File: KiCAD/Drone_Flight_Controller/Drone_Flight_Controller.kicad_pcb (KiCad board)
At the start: 2 copper layers, 85 x 45 mm, 104 parts, among them J201 Conn_01x04, J205 XT60, J207 Conn_01x05, P601 USB_C_Plug_USB2.0, Q201 BC846C, Q202 BC856C, Q203 BC846C, Q204 BC856C, Q205 BC846C, Q206 BC856C, Q207 BC846C, Q208 BC856C, Q401 2N2222A, Q601 BC846C, Q602 BC846C, Q603 BC846C, Q604 BC846C, Q605 BC846C, Q606 BC846C, Q607 BC846C, SW301 SW_Push, U201 AS358, U202 AS358, U205 AS358, U301 DPS368, U302 BNO055, U303 ESP32-WROOM-32, U601 MCP2200-I-SO, U701 LM2576-3.3WT, Y601 CSTNE12M0GH5L000R0

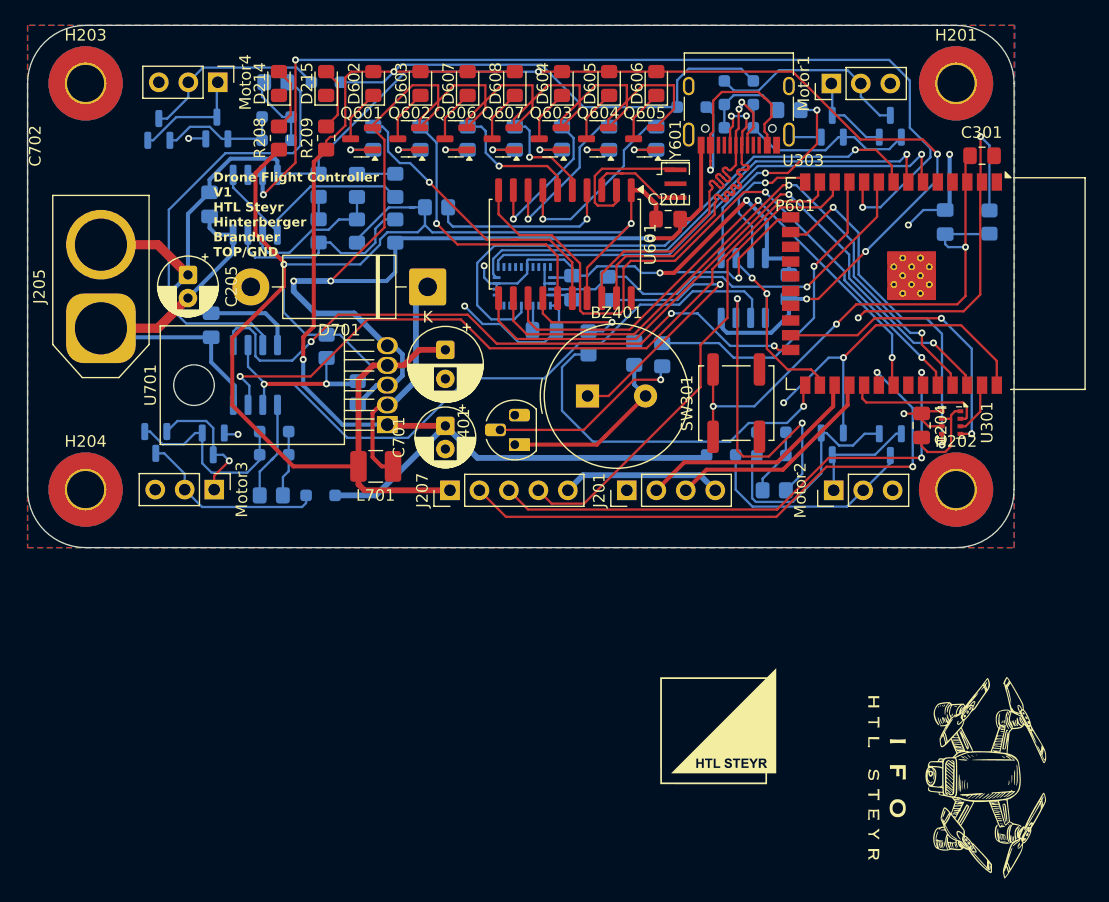
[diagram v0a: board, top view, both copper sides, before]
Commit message: bottom GND and USB C port
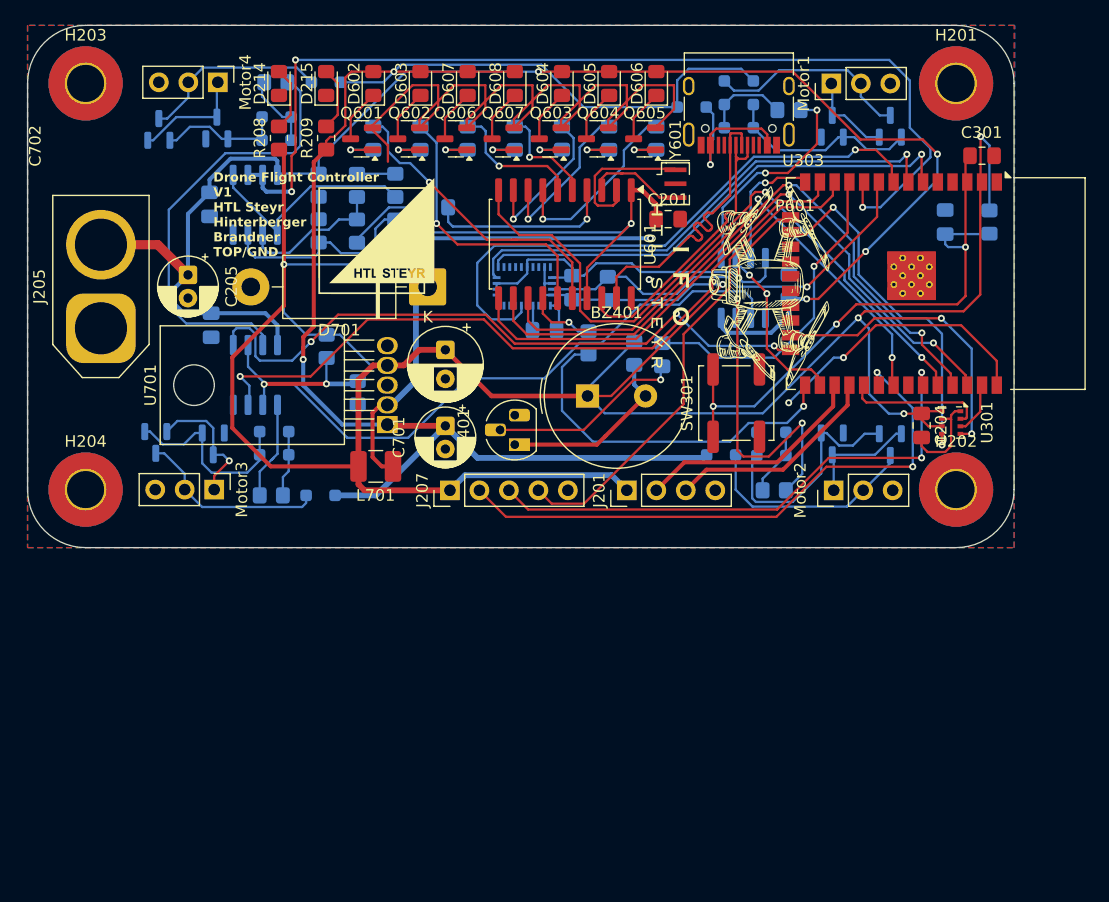
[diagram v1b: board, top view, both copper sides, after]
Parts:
- moved G*** 51.5 mm to (98.0, 93.2)
- moved G*** 46.3 mm to (129.3, 97.3)
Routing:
- net GND: track 325.2 -> 176.3 mm, vias 14 -> 5
- net +3V3: track 204.5 -> 282.0 mm
- net Net-(U601-D-): track 33.2 -> 25.4 mm, vias 2 -> 0
- net Net-(D601-A): track 21.5 -> 14.1 mm
- net Net-(U601-D+): track 31.5 -> 25.9 mm, vias 2 -> 0
- net ~{Programming}: track 9.96 -> 5.89 mm
- net Programming TX: track 60.4 -> 59.2 mm
- net Motor1: track 12.3 -> 11.2 mm
- net BATT Monitor: track 86.5 -> 87.3 mm
- added copper zone on B.Cu, net GND
- removed copper zone on B.Cu, net +3V3

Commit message: add IFO picture and HTL Logo
add IFO picture and HTL Logo
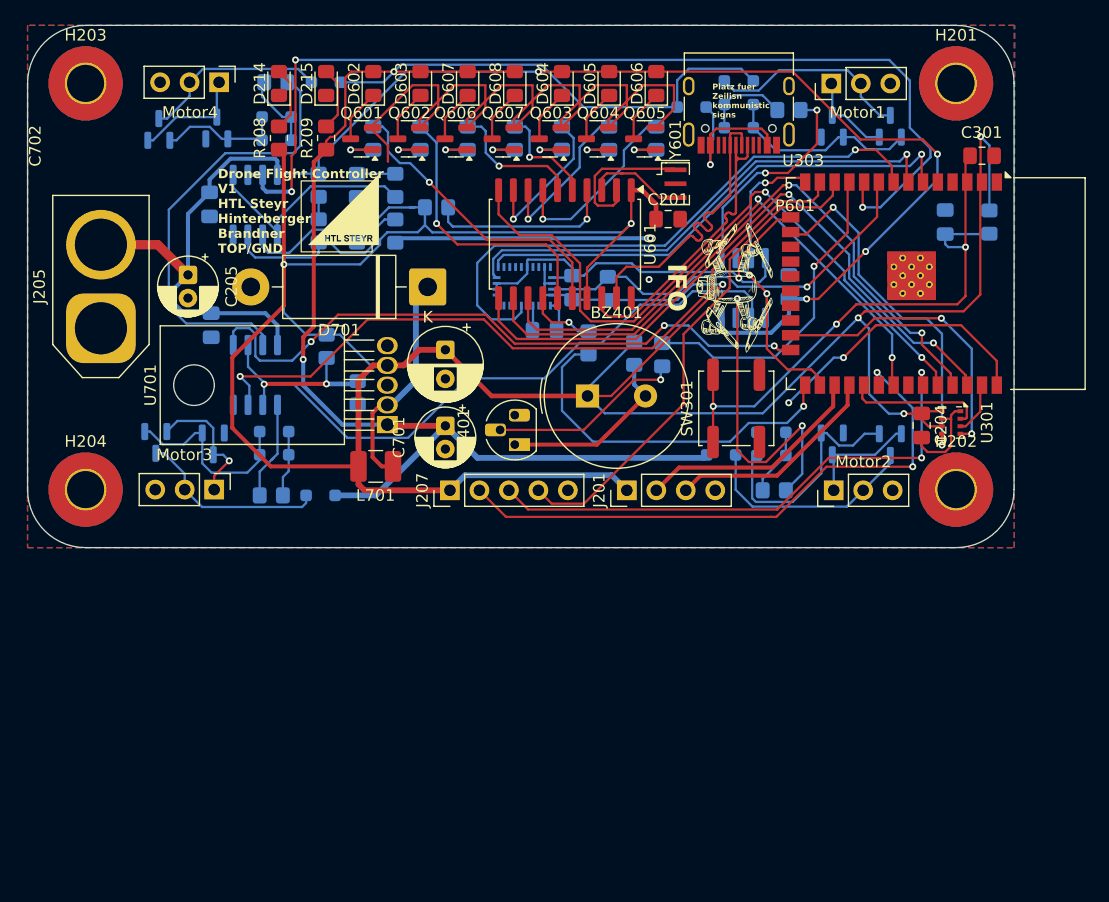
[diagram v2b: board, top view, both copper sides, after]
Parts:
- removed G*** (x2): LOGO, LOGO
- moved SW301 0.45 mm to (129.1, 108.0)
- moved Motor4 0.11 mm to (84.5, 79.9)
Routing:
- net Motor4: track 56.6 -> 55.8 mm
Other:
- board text added: "IFO"
- board text added: "Platz fuer Zeilisn kommunistic signs"

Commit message: Connector and ESP placement
Connector and ESP placement
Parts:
- moved Motor3 0.58 mm to (83.5, 115.0)
- moved U303 0.25 mm to (143.2, 97.5)
- moved Motor1 0.16 mm to (137.4, 80.0)
- moved Motor4 0.12 mm to (84.6, 80.0)
- moved J207 0.12 mm to (104.5, 115.0)
- moved Motor2 0.06 mm to (137.5, 115.0)
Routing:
- net Net-(D201-A): track 17.6 -> 18.4 mm
- net Net-(Motor3-Pin_1): track 11.7 -> 12.3 mm
- net BATT Monitor: track 87.3 -> 87.8 mm

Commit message: diodes
add diodes
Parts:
- added C10: 100n, Capacitor_SMD:C_0805_2012Metric_Pad1.18x1.45mm_HandSolder, F.Cu at (141.5, 83.7)
- added C11: 100n, Capacitor_SMD:C_0805_2012Metric_Pad1.18x1.45mm_HandSolder, F.Cu at (141.1, 109.0)
- added C12: 100n, Capacitor_SMD:C_0805_2012Metric_Pad1.18x1.45mm_HandSolder, F.Cu at (82.0, 112.2)
- added C13: 100n, Capacitor_SMD:C_0805_2012Metric_Pad1.18x1.45mm_HandSolder, F.Cu at (83.1, 86.0)
- added D1: VTVS5V0ASMF-HM3-08, Diode_SMD:D_SMF, F.Cu at (137.9, 84.2)
- added D2: VTVS5V0ASMF-HM3-08, Diode_SMD:D_SMF, F.Cu at (141.5, 112.0)
- added D3: VTVS5V0ASMF-HM3-08, Diode_SMD:D_SMF, F.Cu at (77.8, 110.8)
- added D4: VTVS5V0ASMF-HM3-08, Diode_SMD:D_SMF, F.Cu at (83.5, 83.2)
- added D5: VTVS5V0ASMF-HM3-08, Diode_SMD:D_SMF, B.Cu at (125.3, 88.4)
- moved L701 1.70 mm to (96.3, 112.9)
- moved C201 1.25 mm to (122.1, 92.3), turned to -90 degrees
- moved R203 0.96 mm to (95.5, 106.8)
- moved SW301 0.50 mm to (129.1, 107.5)
- moved Q201 0.40 mm to (142.4, 83.3)
- moved J201 0.25 mm to (119.9, 115.0)
- moved BZ401 0.18 mm to (116.2, 106.8)
- moved J207 0.16 mm to (104.3, 115.0)
- moved C701 0.16 mm to (104.0, 109.3)
- moved U701 0.10 mm to (99.0, 109.3)
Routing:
- net GND: track 176.5 -> 151.9 mm, vias 5 -> 10
- net Net-(D1-K): track 18.4 -> 25.3 mm
- net IO1: track 50.8 -> 44.7 mm
- net Net-(D2-K): track 19.1 -> 25.1 mm
- net Net-(D207-A): track 16.8 -> 22.7 mm
- net Net-(D210-A): track 17.0 -> 22.9 mm
- net Motor4: track 55.9 -> 58.8 mm
- net Net-(U601-D-): track 25.4 -> 27.9 mm
- net IO2: track 46.8 -> 44.9 mm
- net +3V3: track 282.4 -> 281.0 mm
- net Net-(D5-K): track 14.1 -> 15.6 mm
- net +4V76: track 133.3 -> 134.5 mm
- net +BATT: track 132.6 -> 133.8 mm
- net +1V7: track 67.2 -> 66.2 mm
- net Net-(U601-D+): track 25.9 -> 26.9 mm
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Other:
- board text added: "Drone Flight Controller V2 HTL Steyr Hinterberger Brandner TOP/GND"
- board text removed: "Drone Flight Controller V1 HTL Steyr Hinterberger Brandner TOP/GND"

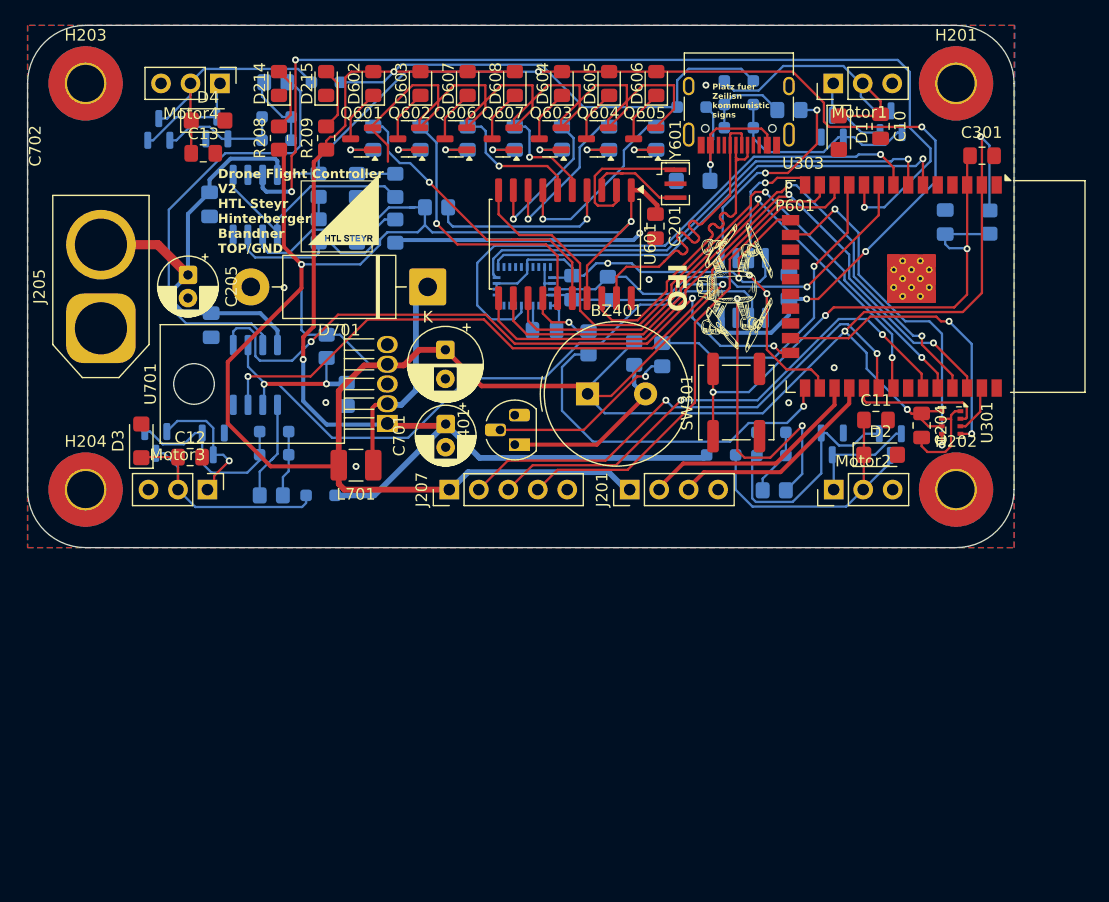
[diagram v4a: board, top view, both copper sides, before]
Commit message: solve routing errors
solve routing errors
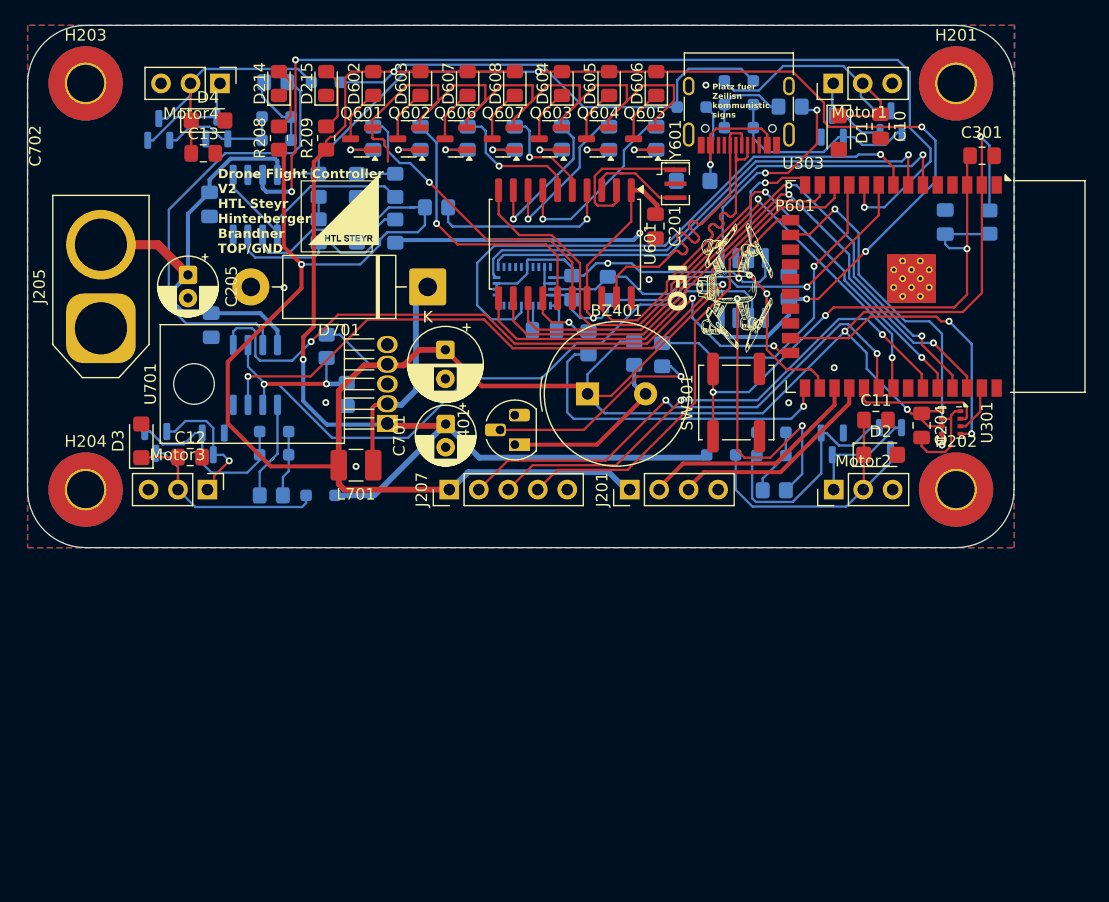
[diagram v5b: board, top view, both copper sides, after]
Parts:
- moved Q203 0.52 mm to (142.3, 110.6)
- moved R201 0.31 mm to (133.7, 82.0)
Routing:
- net +3V3: track 281.0 -> 259.6 mm
- net GND: track 151.9 -> 148.6 mm
- net Net-(Q401-B): track 16.5 -> 19.5 mm
- net Net-(U303-IO0): track 31.3 -> 29.1 mm
- net Motor1: track 11.4 -> 10.6 mm
- net +BATT: track 133.8 -> 134.3 mm
- net Net-(D2-K): track 25.1 -> 25.7 mm

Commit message: improving routing
improving routing
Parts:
- moved R202 1.06 mm to (94.8, 102.2)
- moved R203 0.75 mm to (94.8, 106.8)
- moved C304 0.48 mm to (112.2, 101.6)
- moved U302 0.43 mm to (110.4, 97.6)
- moved SW301 0.36 mm to (128.7, 107.5)
- moved R402 0.28 mm to (122.9, 103.2)
- moved BZ401 0.25 mm to (116.2, 106.5)
- moved C302 0.08 mm to (115.0, 97.7)
- moved R603 0.08 mm to (101.9, 84.8)
- turned D201 to 0 degrees
- turned D202 to 180 degrees
- turned D203 to 0 degrees
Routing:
- net GND: track 148.6 -> 36.2 mm, vias 10 -> 8
- net BATT Monitor: track 87.6 -> 83.4 mm
- net Net-(D1-K): track 25.3 -> 21.7 mm
- net Net-(U301-SDO): track 31.3 -> 27.9 mm
- net Net-(D202-K): track 7.40 -> 4.24 mm
- net Net-(Q401-B): track 19.5 -> 16.5 mm
- net +BATT: track 134.3 -> 132.2 mm
- net Net-(D202-A): track 17.5 -> 19.4 mm
- net Net-(U301-SCK): track 26.1 -> 24.8 mm
- net Net-(U302-COM1): track 43.7 -> 44.7 mm
- net +3V3: track 259.6 -> 260.6 mm
- net Net-(R206-Pad1): track 38.7 -> 37.8 mm
- net Net-(U601-GP1/USB-CFG): track 24.1 -> 23.3 mm
- net Net-(U302-~{RESET}): track 50.3 -> 51.1 mm
- net Net-(Motor3-Pin_1): track 12.3 -> 11.8 mm

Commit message: routing
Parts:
- moved D207 1.16 mm to (93.1, 114.3)
- moved R205 1.15 mm to (89.0, 114.3)
- moved R204 0.59 mm to (132.5, 114.5)
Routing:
- net GND: track 36.2 -> 26.3 mm
- net Net-(D208-K): track 5.71 -> 4.13 mm
- net Net-(U601-D-): track 27.9 -> 26.5 mm
- net Net-(R205-Pad1): track 8.62 -> 7.32 mm
- net BATT Monitor: track 83.4 -> 82.4 mm
- net Net-(R201-Pad1): track 19.7 -> 18.8 mm
- net +4V76: track 134.6 -> 133.8 mm
- net +BATT: track 132.2 -> 131.6 mm
- net Net-(Motor4-Pin_1): track 10.0 -> 9.39 mm
- net +1V7: track 66.5 -> 65.9 mm
- net Net-(D205-A): track 22.5 -> 22.0 mm
- net Net-(D207-A): track 22.5 -> 23.0 mm
